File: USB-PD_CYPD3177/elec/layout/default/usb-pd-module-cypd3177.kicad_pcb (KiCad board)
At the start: 2 copper layers, 40 x 40 mm, 72 parts

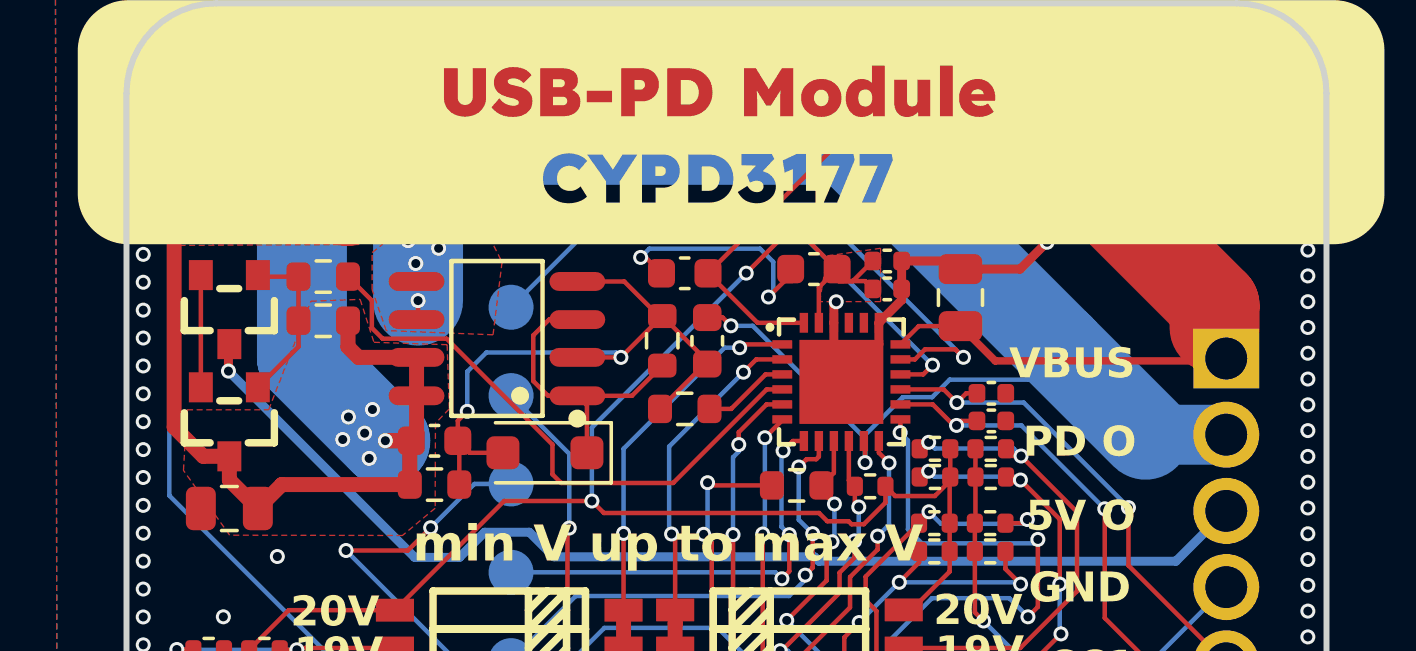
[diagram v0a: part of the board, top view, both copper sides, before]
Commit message: updated layout
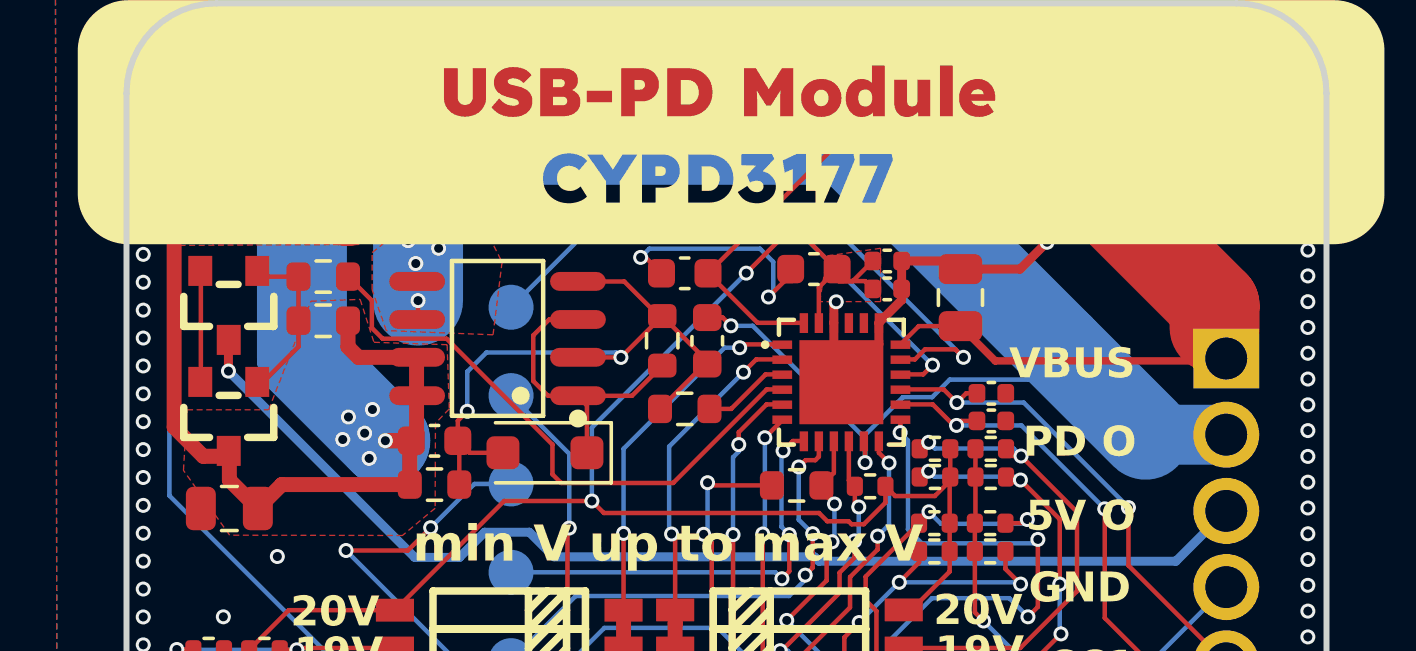
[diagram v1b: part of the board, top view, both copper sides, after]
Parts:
- removed the U1 at (173.2, 89.3)
- removed the U2 at (161.7, 87.8)
- removed the U3 at (152.8, 90.6)
- removed the U4 at (152.8, 86.9)
- added Q1: , lib:SOP-8_L4.9-W3.9-P1.27-LS6.0-BL, F.Cu at (161.7, 87.8)
- added Q2: , lib:SOT-23_L2.9-W1.3-P1.90-LS2.4-BR, F.Cu at (152.8, 90.4)
- added Q3: , lib:SOT-23_L2.9-W1.3-P1.90-LS2.4-BR, F.Cu at (152.8, 86.7)
- added U20: , lib:TQFN-24_L4.0-W4.0-P0.50-TL-EP2.8, F.Cu at (173.2, 89.3)
- C1, C6: value 3.3uF +/- 10% -> 16V 3.3uF X7R ±10% 0805 Multilayer Ceramic Capacitors MLCC - SMD/SMT ROHS
- C10, C9: value 0.1uF +/- 10% -> 16V 100nF X7R ±10% 0402 Multilayer Ceramic Capacitors MLCC - SMD/SMT ROHS
- C2, C3, C7, C8: value 1uF +/- 10% -> 50V 1uF X5R ±10% 0603 Multilayer Ceramic Capacitors MLCC - SMD/SMT ROHS
- C4: value 390pF +/- 5% -> 50V 390pF NP0 ±5% 0402 Multilayer Ceramic Capacitors MLCC - SMD/SMT ROHS
- R1: value 10kohm +/- 1% -> 100mW Thick Film Resistors 75V ±100ppm/℃ ±1% 10kΩ 0603 Chip Resistor - Surface Mount ROHS
- R10, R12, R13, R14, R16, R18, R20, R21, R22, R24, R26, R28, R29, R30, R32, R34, R36, R37, R8: value 5.1kohm +/- 1% -> 62.5mW Thick Film Resistors 50V ±100ppm/℃ ±1% 5.1kΩ 0402 Chip Resistor - Surface Mount ROHS
- R11, R19, R27, R35: value 2.4kohm +/- 1% -> 62.5mW Thick Film Resistors 50V ±100ppm/℃ ±1% 2.4kΩ 0402 Chip Resistor - Surface Mount ROHS
- R15, R23, R31: value 10kohm +/- 1% -> 62.5mW Thick Film Resistors 50V ±100ppm/℃ ±1% 10kΩ 0402 Chip Resistor - Surface Mount ROHS
- R17, R25, R33, R9: value 1kohm +/- 1% -> 62.5mW Thick Film Resistors 50V ±100ppm/℃ ±1% 1kΩ 0402 Chip Resistor - Surface Mount ROHS
- R2, R5: value 1kohm +/- 1% -> 100mW Thick Film Resistors 75V ±100ppm/℃ ±1% 1kΩ 0603 Chip Resistor - Surface Mount ROHS
- R3, R4: value 49.9kohm +/- 1% -> 100mW Thick Film Resistors 75V ±100ppm/℃ ±1% 49.9kΩ 0603 Chip Resistor - Surface Mount ROHS
- R6: value 100kohm +/- 5% -> 100mW Thick Film Resistors 75V ±100ppm/℃ ±1% 100kΩ 0603 Chip Resistor - Surface Mount ROHS
- R7: value 2kohm +/- 1% -> 62.5mW Thick Film Resistors 50V ±100ppm/℃ ±1% 2kΩ 0402 Chip Resistor - Surface Mount ROHS
- renumbered U5 to U1, U14 to U10, U15 to U11, U16 to U12, U17 to U13, U18 to U14, U19 to U15, U20 to U16, U21 to U17, U22 to U18, U23 to U19, U6 to U2, U7 to U3, U8 to U4, U9 to U5, U10 to U6, U11 to U7, U12 to U8, U13 to U9
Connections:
- net power_out_vbus_load_switch.load_switch_mosfet-gnd renamed power_out_vbus_load_switch.dual_p_mosfet-gnd
- net source1 renamed power_out_vbus_load_switch.dual_p_mosfet-source
- net vcc-1 renamed vdc_out
- net vcc-3 renamed vddd
- net vcc-4 renamed vccd
- C1 pad 1: vcc -> vbus_in
- C2 pad 1: vcc -> vbus_in
- C6 pad 1: vcc -> vbus_in
- R1 pad 1: vcc -> vbus_in
- R4 pad 1: vcc -> vbus_in
- U5 pad 1: vcc -> vbus_in
- U5 pad 3: vcc-2 -> vcc
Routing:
- net vbus_in: track 0.00 -> 85.5 mm, vias 0 -> 11
- net vcc: track 85.5 -> 38.2 mm, vias 11 -> 1
- net vcc-2: track 38.2 -> 0.00 mm, vias 1 -> 0
- net source: track 3.74 -> 0.00 mm
- net power_out_5v_load_switch.p_mosfet_1-source: track 0.00 -> 3.74 mm
- added copper zone on F.Cu, net vbus_in
- removed copper zone on F.Cu, net vcc
